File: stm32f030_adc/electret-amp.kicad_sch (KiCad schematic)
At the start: 9 parts, among them Q1 2N3904

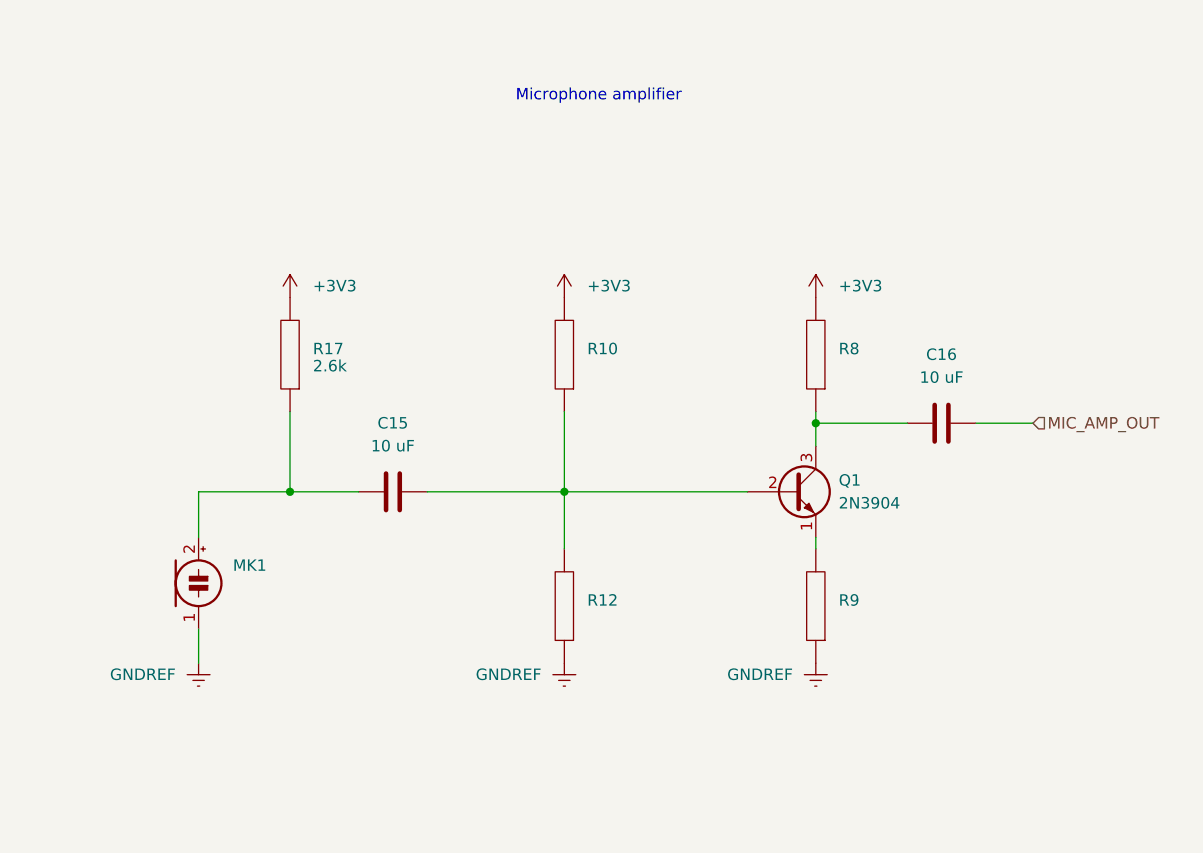
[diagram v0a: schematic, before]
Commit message: [bjt-amp-calc bjt-amp-simulation schematics] Impl | Validated amplifier design
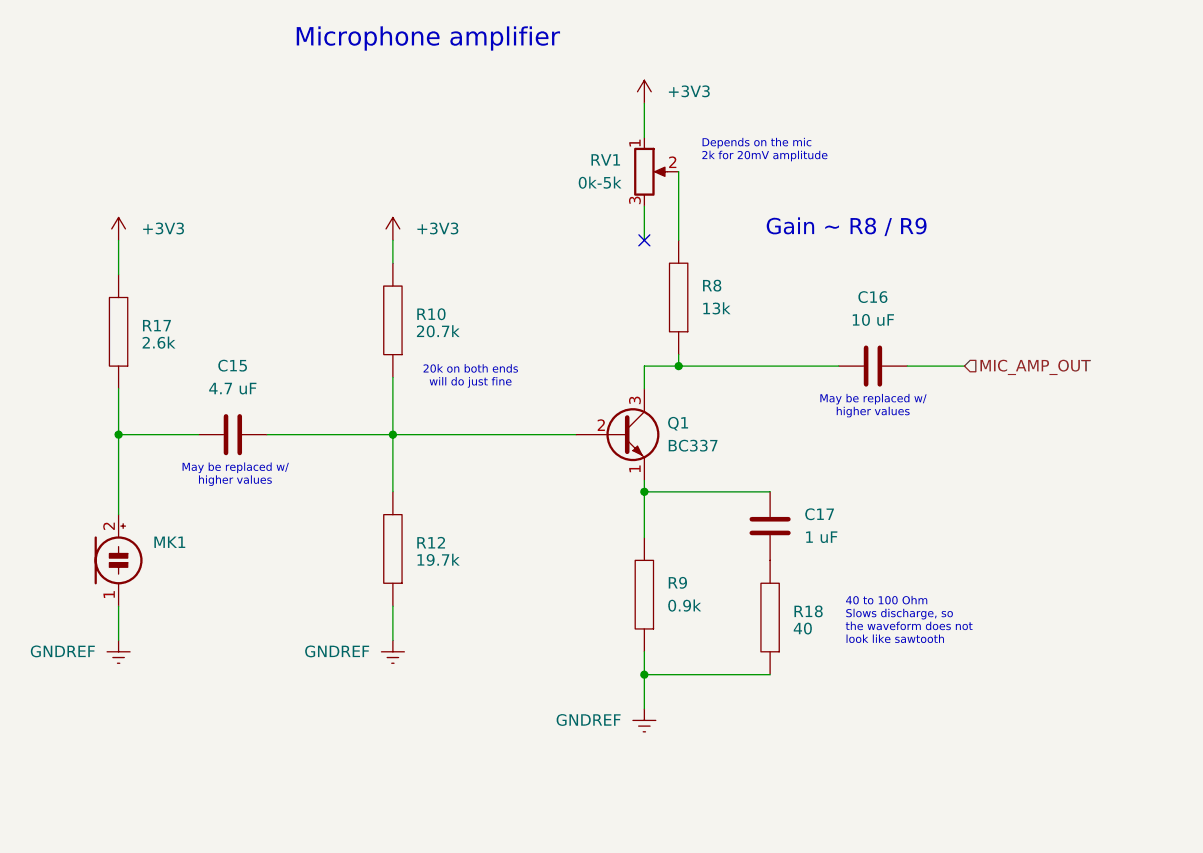
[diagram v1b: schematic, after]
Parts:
- added C17: 1 uF, symbol Device:C
- added R18: 40, symbol pspice:R
- added RV1: 0k-5k, symbol Device:R_Potentiometer
- C15: value 10 uF -> 4.7 uF
- Q1: value 2N3904 -> BC337
- R10: value ~ -> 20.7k
- R12: value ~ -> 19.7k
- R8: value ~ -> 13k
- R9: value ~ -> 0.9k
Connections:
- net +3V3: now also RV1.1; no longer R8.2
- net GNDREF: now also R18.1
- net at Q1.1 (E), R9.2: now also C17.2
- new net: R8.2, RV1.2
- new net: C17.1, R18.2
- no-connect marks 0 -> 1
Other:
- note added: "20k on both ends will do just fine"
- note added: "40 to 100 Ohm Slows discharge, so the waveform does not look like sawtooth"
- note added: "Depends on the mic 2k for 20mV amplitude"
- note added: "Gain ~ R8 / R9"
- note added: "May be replaced w/ higher values"
- moved on the sheet: C15, C16, MK1, Q1, R10, R12, R17, R8, R9

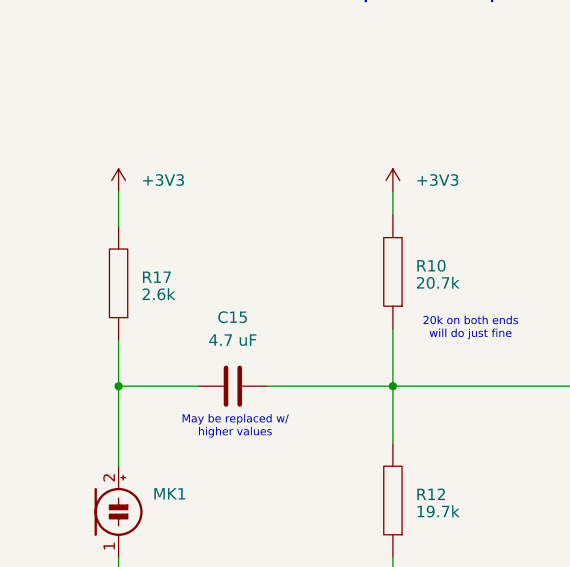
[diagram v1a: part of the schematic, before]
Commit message: [schematics] Enh | Verified microphone design on a prototype hardware, adjusted mic. power resistance
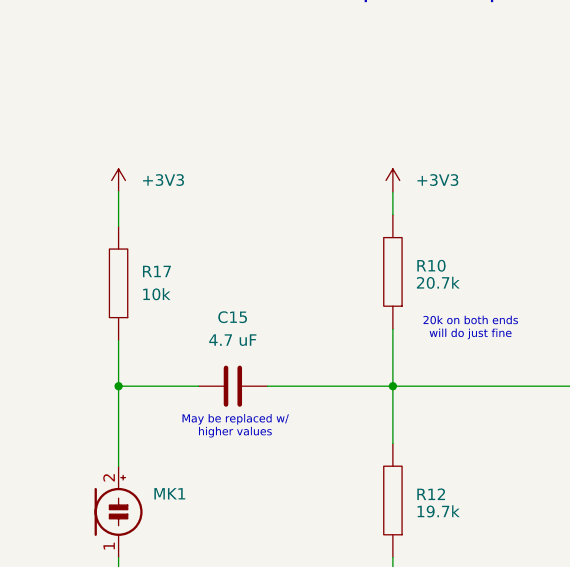
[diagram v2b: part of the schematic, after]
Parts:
- R17: value 2.6k -> 10k
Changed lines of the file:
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@@
 		(fields_autoplaced yes)
 		(property "Reference" "R17"
-			(at 97.79 88.2649 0)
+			(at 97.79 87.6299 0)
 			(effects
 				(font
@@
 			)
 		)
-		(property "Value" "2.6k"
-			(at 97.79 90.17 0)
+		(property "Value" "10k"
+			(at 97.79 90.1699 0)
 			(effects
 				(font

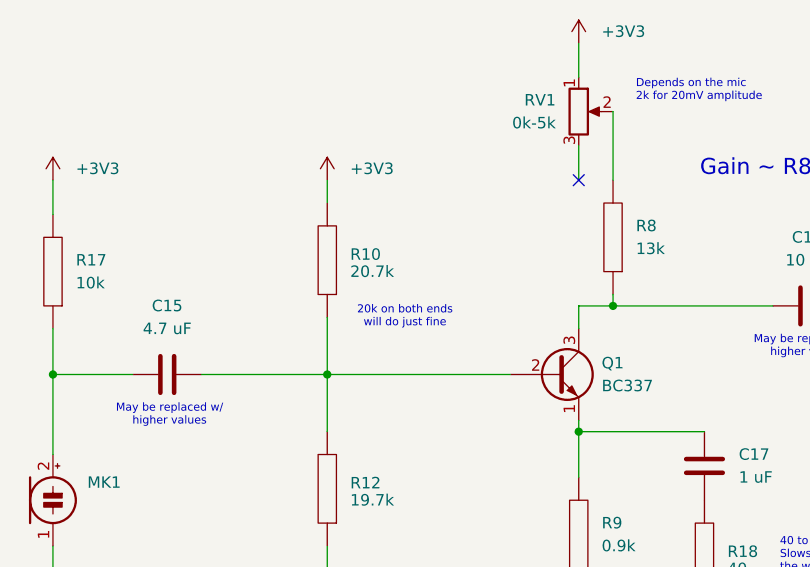
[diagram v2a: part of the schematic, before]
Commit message: [schematics] Bug | Wrong resistor values to offset the gate
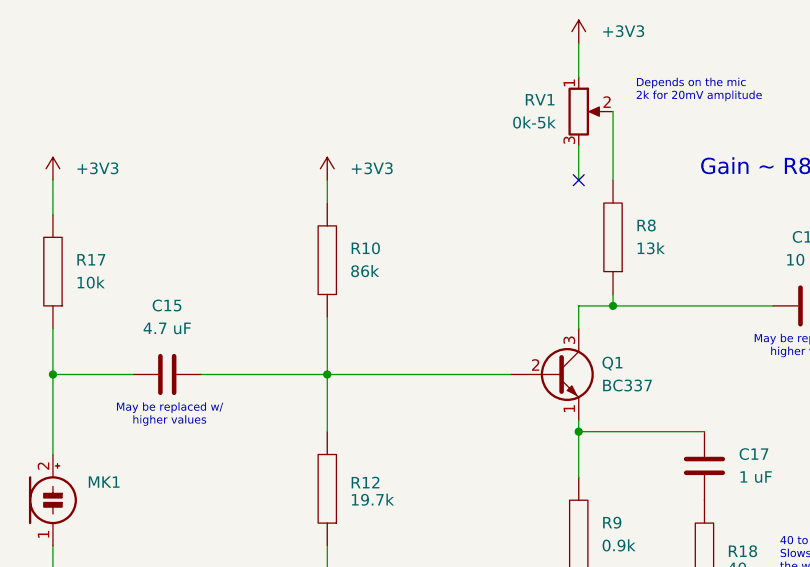
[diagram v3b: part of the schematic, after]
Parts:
- R10: value 20.7k -> 86k
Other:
- note removed: "20k on both ends will do just fine"
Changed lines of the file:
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@@
-		)
-	)
-	(text "20k on both ends\nwill do just fine"
-		(exclude_from_sim no)
-		(at 134.366 93.98 0)
-		(effects
-			(font
-				(size 0.889 0.889)
-			)
 		)
 	)
@@
 		(fields_autoplaced yes)
 		(property "Reference" "R10"
-			(at 128.27 86.9949 0)
-			(effects
-				(font
-					(size 1.27 1.27)
-				)
-				(justify right)
-			)
-		)
-		(property "Value" "20.7k"
-			(at 128.27 88.9 0)
-			(effects
-				(font
+			(at 128.27 86.3599 0)
+			(effects
+				(font
+					(size 1.27 1.27)
+				)
+				(justify right)
+			)
+		)
+		(property "Value" "86k"
+			(at 128.27 88.8999 0)
+			(effects
+				(font

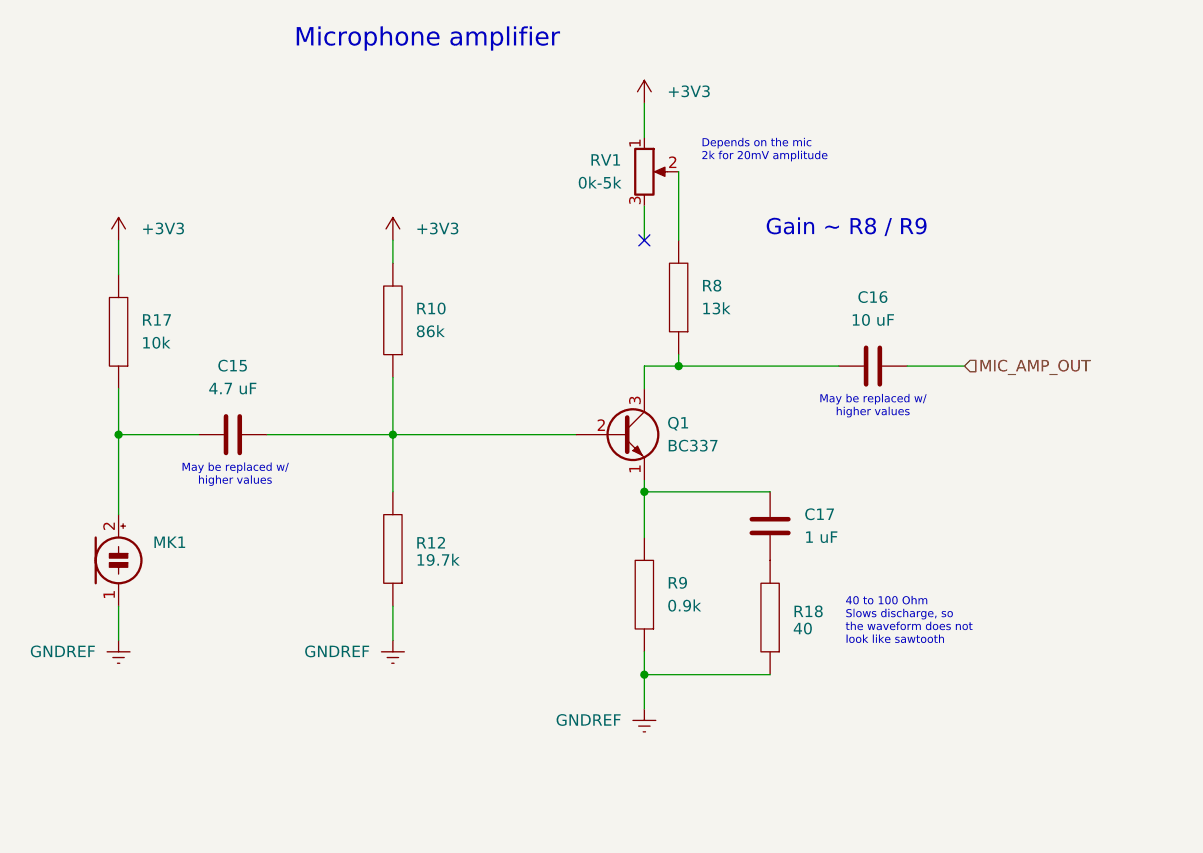
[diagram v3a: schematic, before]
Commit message: [bjt-amp-calc schematics] Enh | Modified consulting the prototype
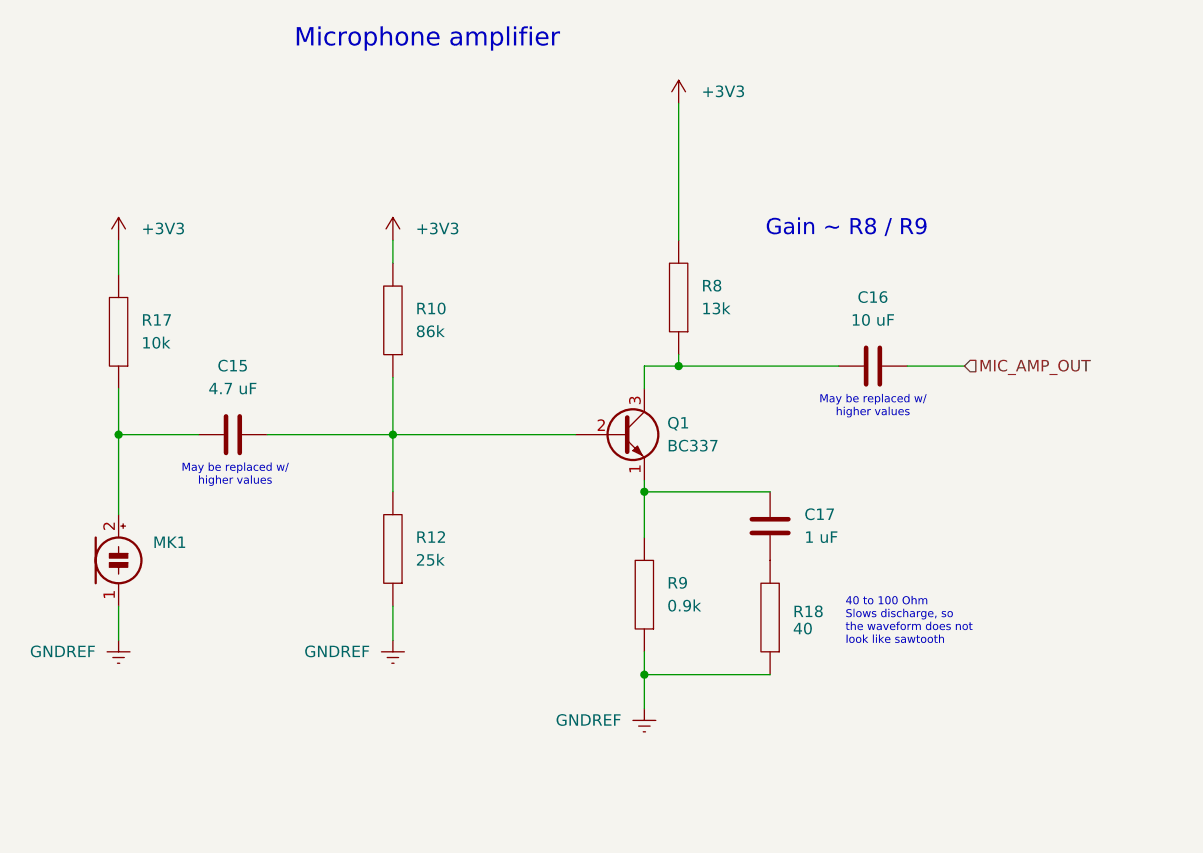
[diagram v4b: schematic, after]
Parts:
- removed RV1: 0k-5k, symbol Device:R_Potentiometer
- R12: value 19.7k -> 25k
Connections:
- net +3V3: now also R8.2
- no-connect marks 1 -> 0
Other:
- note removed: "Depends on the mic 2k for 20mV amplitude"
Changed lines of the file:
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@@
 		(color 0 0 0 0)
 	)
-	(no_connect
-		(at 153.67 78.74)
-	)
 	(wire
 		(pts
@@
 	(wire
 		(pts
-			(xy 157.48 71.12) (xy 157.48 78.74)
-		)
-		(stroke
-			(width 0)
-			(type default)
-		)
-	)
-	(wire
-		(pts
 			(xy 95.25 100.33) (xy 104.14 100.33)
 		)
@@
 	(wire
 		(pts
-			(xy 153.67 63.5) (xy 153.67 67.31)
+			(xy 157.48 63.5) (xy 157.48 78.74)
 		)
 		(stroke
@@
 	(wire
 		(pts
-			(xy 153.67 74.93) (xy 153.67 78.74)
-		)
-		(stroke
-			(width 0)
-			(type default)
-		)
-	)
-	(wire
-		(pts
 			(xy 153.67 105.41) (xy 153.67 106.68)
 		)
@@
 			(width 0)
 			(type default)
-		)
-	)
-	(text "Depends on the mic\n2k for 20mV amplitude"
-		(exclude_from_sim no)
-		(at 160.02 68.834 0)
-		(effects
-			(font
-				(size 0.889 0.889)
-			)
-			(justify left)
 		)
 	)
@@
 	(symbol
 		(lib_id "power:+3V3")
-		(at 153.67 63.5 0)
+		(at 157.48 63.5 0)
 		(unit 1)
 		(exclude_from_sim no)
@@
 		(fields_autoplaced yes)
 		(property "Reference" "#PWR010"
-			(at 153.67 67.31 0)
+			(at 157.48 67.31 0)
 			(effects
 				(font
@@
 		)
 		(property "Value" "+3V3"
-			(at 156.21 62.2299 0)
+			(at 160.02 62.2299 0)
 			(effects
 				(font
@@
 		)
 		(property "Footprint" ""
-			(at 153.67 63.5 0)
+			(at 157.48 63.5 0)
 			(effects
 				(font
@@
 		)
 		(property "Datasheet" ""
-			(at 153.67 63.5 0)
+			(at 157.48 63.5 0)
 			(effects
 				(font
@@
 		)
 		(property "Description" ""
-			(at 153.67 63.5 0)
+			(at 157.48 63.5 0)
 			(effects
 				(font
@@
 		(fields_autoplaced yes)
 		(property "Reference" "R12"
-			(at 128.27 112.3949 0)
-			(effects
-				(font
-					(size 1.27 1.27)
-				)
-				(justify right)
-			)
-		)
-		(property "Value" "19.7k"
-			(at 128.27 114.3 0)
+			(at 128.27 111.7599 0)
+			(effects
+				(font
+					(size 1.27 1.27)
+				)
+				(justify right)
+			)
+		)
+		(property "Value" "25k"
+			(at 128.27 114.2999 0)
 			(effects
 				(font
@@
 					(unit 1)
 				)
-			)
-		)
-	)
-	(symbol
-		(lib_id "Device:R_Potentiometer")
-		(at 153.67 71.12 0)
-		(unit 1)
-		(exclude_from_sim no)
-		(in_bom yes)
-		(on_board yes)
-		(dnp no)
-		(fields_autoplaced yes)
-		(property "Reference" "RV1"
-			(at 151.13 69.8499 0)
-			(effects
-				(font
-					(size 1.27 1.27)
-				)
-				(justify right)
-			)
-		)
-		(property "Value" "0k-5k"
-			(at 151.13 72.3899 0)
-			(effects
-				(font
-					(size 1.27 1.27)
-				)
-				(justify right)
-			)
-		)
-		(property "Footprint" ""
-			(at 153.67 71.12 0)
-			(effects
-				(font
-					(size 1.27 1.27)
-				)
-				(hide yes)
-			)
-		)
-		(property "Datasheet" "~"
-			(at 153.67 71.12 0)
-			(effects
-				(font
-					(size 1.27 1.27)
-				)
-				(hide yes)
-			)
-		)
-		(property "Description" "Potentiometer"
-			(at 153.67 71.12 0)
-			(effects
-				(font
-					(size 1.27 1.27)
-				)
-				(hide yes)
-			)
-		)
-		(pin "2"
-		)
-		(pin "1"
-		)
-		(pin "3"
-		)
-		(instances
-			(project ""
-				(path "/85629656-c73b-4e1f-b8e8-4366f4b01266/f519304b-9da7-41e0-88ca-532cf10653e0"
-					(reference "RV1")
-					(unit 1)
-				)

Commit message: Assigned footprints, removed obsolete parts
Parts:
- C15, C16, C17: footprint (none) -> Capacitor_THT:CP_Axial_L10.0mm_D4.5mm_P15.00mm_Horizontal
- MK1, R10, R12, R17, R18, R8, R9: footprint (none) -> Resistor_THT:R_Axial_DIN0207_L6.3mm_D2.5mm_P10.16mm_Horizontal
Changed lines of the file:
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@@
 			)
 		)
-		(property "Footprint" ""
+		(property "Footprint" "Resistor_THT:R_Axial_DIN0207_L6.3mm_D2.5mm_P10.16mm_Horizontal"
 			(at 157.48 85.09 0)
 			(effects
@@
 			)
 		)
-		(property "Footprint" ""
+		(property "Footprint" "Capacitor_THT:CP_Axial_L10.0mm_D4.5mm_P15.00mm_Horizontal"
 			(at 111.76 99.3648 0)
 			(effects
@@
 			)
 		)
-		(property "Footprint" ""
+		(property "Footprint" "Capacitor_THT:CP_Axial_L10.0mm_D4.5mm_P15.00mm_Horizontal"
 			(at 166.6748 106.68 0)
 			(effects
@@
 			)
 		)
-		(property "Footprint" ""
+		(property "Footprint" "Capacitor_THT:CP_Axial_L10.0mm_D4.5mm_P15.00mm_Horizontal"
 			(at 182.88 91.7448 0)
 			(effects
@@
 			)
 		)
-		(property "Footprint" ""
+		(property "Footprint" "Resistor_THT:R_Axial_DIN0207_L6.3mm_D2.5mm_P10.16mm_Horizontal"
 			(at 167.64 120.65 0)
 			(effects
@@
 			)
 		)
-		(property "Footprint" ""
+		(property "Footprint" "Resistor_THT:R_Axial_DIN0207_L6.3mm_D2.5mm_P10.16mm_Horizontal"
 			(at 95.25 88.9 0)
 			(effects
@@
 			)
 		)
-		(property "Footprint" ""
+		(property "Footprint" "Resistor_THT:R_Axial_DIN0207_L6.3mm_D2.5mm_P10.16mm_Horizontal"
 			(at 153.67 118.11 0)
 			(effects
@@
 			)
 		)
-		(property "Footprint" ""
+		(property "Footprint" "Resistor_THT:R_Axial_DIN0207_L6.3mm_D2.5mm_P10.16mm_Horizontal"
 			(at 95.25 111.76 90)
 			(effects
@@
 			)
 		)
-		(property "Footprint" ""
+		(property "Footprint" "Resistor_THT:R_Axial_DIN0207_L6.3mm_D2.5mm_P10.16mm_Horizontal"
 			(at 125.73 113.03 0)
 			(effects
@@
 			)
 		)
-		(property "Footprint" ""
+		(property "Footprint" "Resistor_THT:R_Axial_DIN0207_L6.3mm_D2.5mm_P10.16mm_Horizontal"
 			(at 125.73 87.63 0)
 			(effects

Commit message: [schematics] Build | Changed oscillator type, fixed unconnected lines, made some layout
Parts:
- C17: footprint Capacitor_THT:CP_Axial_L10.0mm_D4.5mm_P15.00mm_Horizontal -> Capacitor_THT:C_Disc_D4.7mm_W2.5mm_P5.00mm
- MK1: footprint Resistor_THT:R_Axial_DIN0207_L6.3mm_D2.5mm_P10.16mm_Horizontal -> Connector_PinSocket_2.00mm:PinSocket_1x02_P2.00mm_Vertical
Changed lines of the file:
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@@
 			)
 		)
-		(property "Footprint" "Capacitor_THT:CP_Axial_L10.0mm_D4.5mm_P15.00mm_Horizontal"
+		(property "Footprint" "Capacitor_THT:C_Disc_D4.7mm_W2.5mm_P5.00mm"
 			(at 166.6748 106.68 0)
 			(effects
@@
 			)
 		)
-		(property "Footprint" "Resistor_THT:R_Axial_DIN0207_L6.3mm_D2.5mm_P10.16mm_Horizontal"
+		(property "Footprint" "Connector_PinSocket_2.00mm:PinSocket_1x02_P2.00mm_Vertical"
 			(at 95.25 111.76 90)
 			(effects

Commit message: [schematics] Impl |  Most of the work is done. Intermediate result
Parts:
- C15, C16: footprint Capacitor_THT:CP_Axial_L10.0mm_D4.5mm_P15.00mm_Horizontal -> Capacitor_THT:CP_Radial_D8.0mm_P3.80mm
- C17: footprint Capacitor_THT:C_Disc_D4.7mm_W2.5mm_P5.00mm -> Capacitor_THT:CP_Radial_D8.0mm_P3.80mm
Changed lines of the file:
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@@
 			)
 		)
-		(property "Footprint" "Capacitor_THT:CP_Axial_L10.0mm_D4.5mm_P15.00mm_Horizontal"
+		(property "Footprint" "Capacitor_THT:CP_Radial_D8.0mm_P3.80mm"
 			(at 111.76 99.3648 0)
 			(effects
@@
 			)
 		)
-		(property "Footprint" "Capacitor_THT:C_Disc_D4.7mm_W2.5mm_P5.00mm"
+		(property "Footprint" "Capacitor_THT:CP_Radial_D8.0mm_P3.80mm"
 			(at 166.6748 106.68 0)
 			(effects
@@
 			)
 		)
-		(property "Footprint" "Capacitor_THT:CP_Axial_L10.0mm_D4.5mm_P15.00mm_Horizontal"
+		(property "Footprint" "Capacitor_THT:CP_Radial_D8.0mm_P3.80mm"
 			(at 182.88 91.7448 0)
 			(effects
